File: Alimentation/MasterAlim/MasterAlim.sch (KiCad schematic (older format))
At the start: 37 parts, among them J1 Ext-Con, J10 Batt GND, J11 AU Logic, J2 Alim logique, J3 Batt IN, J4 Reg 1, J5 Batt +, J6 Reg 3, J7 Reg 4, J8 Reg 1, J9 Reg 2, U1 74LS33, U3 ACS712xLCTR-20A

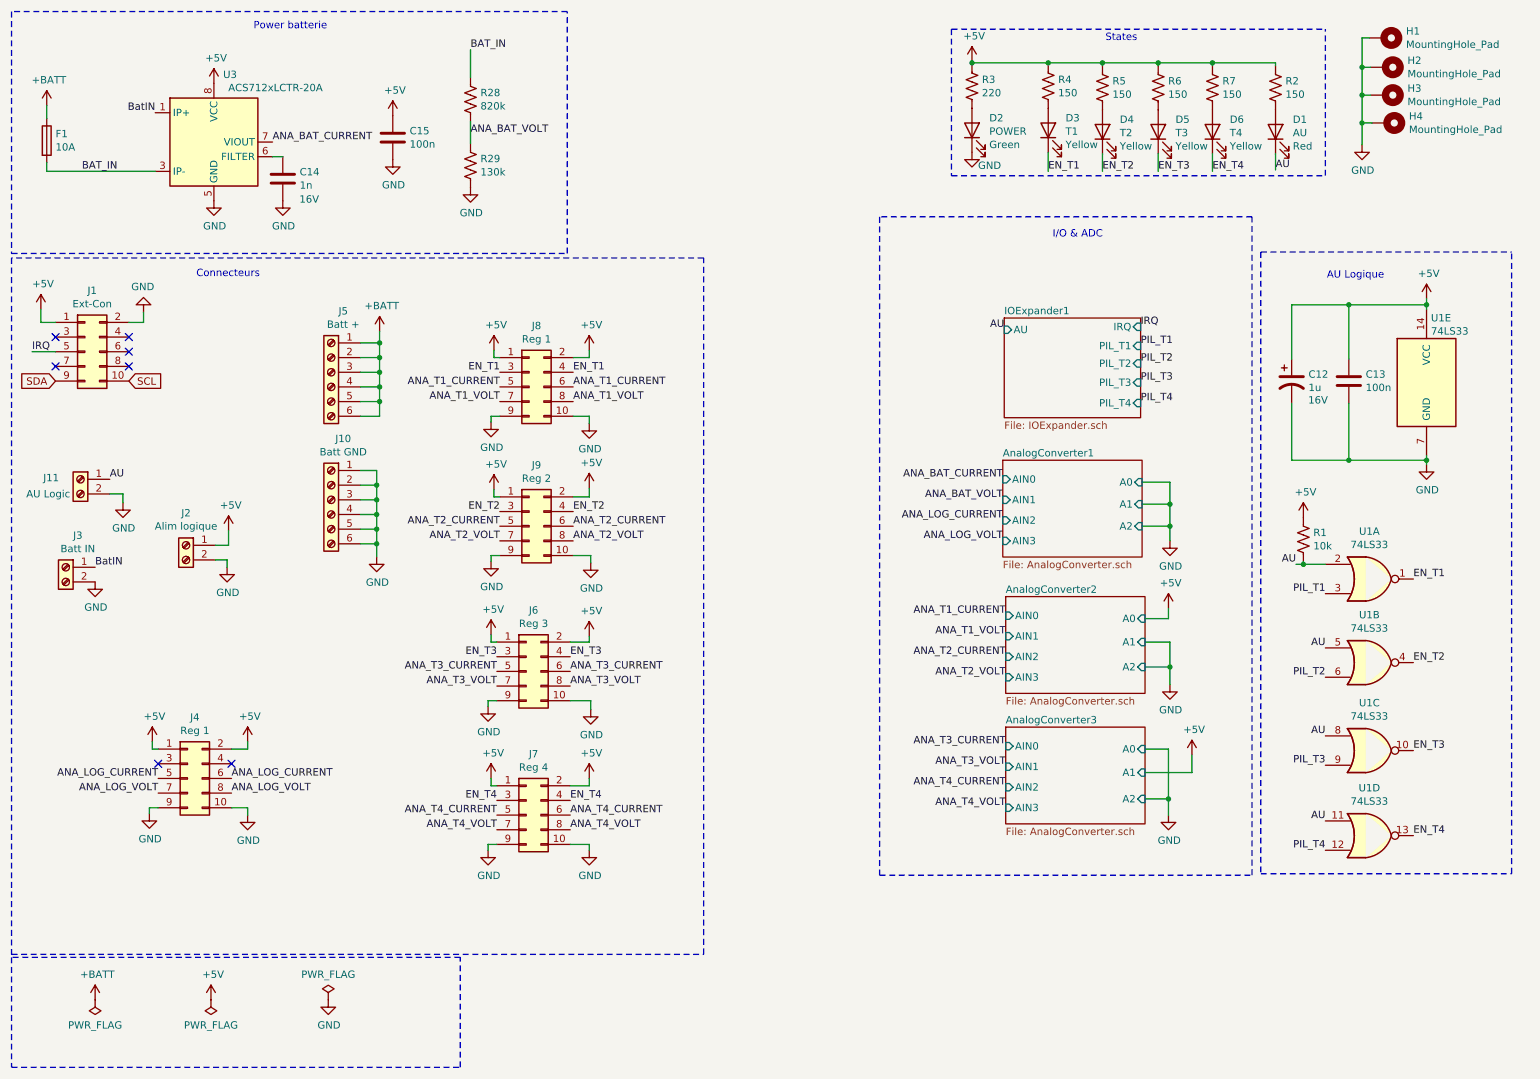
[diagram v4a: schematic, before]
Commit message: Finalisation modules 3A et 6A, routage master alim
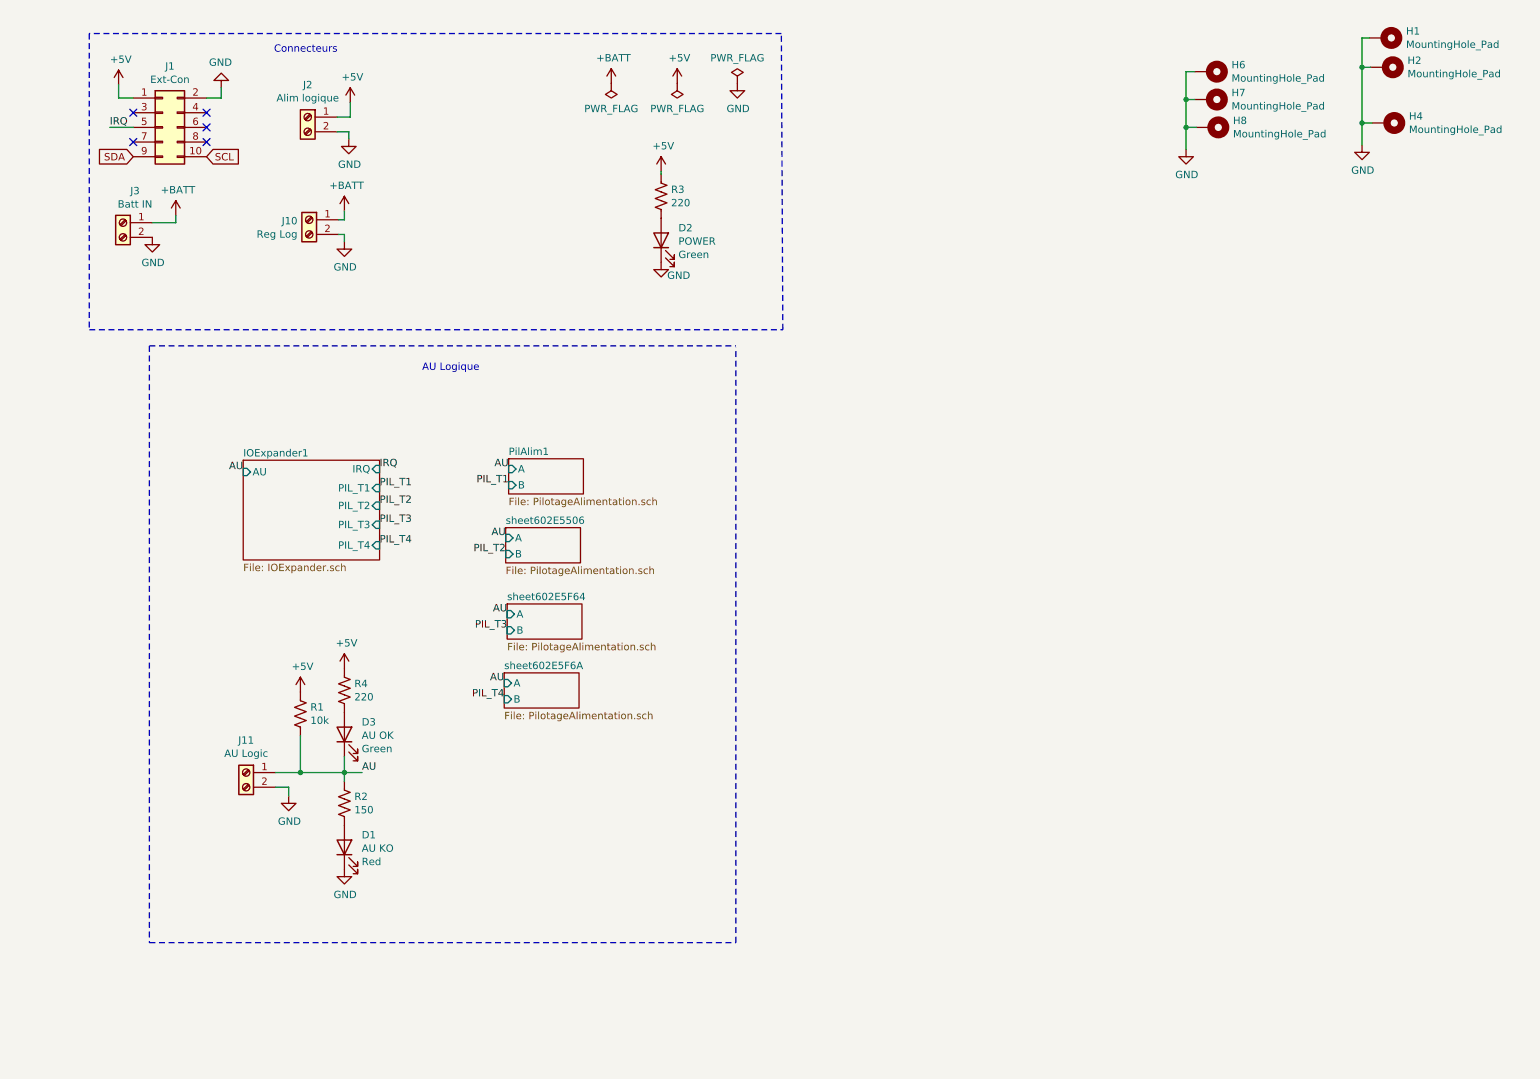
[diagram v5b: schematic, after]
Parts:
- removed C12: 1u, Capacitor_SMD:CP_Elec_4x5.3, symbol Device:CP1
- removed C13, C15: 100n, Capacitor_SMD:C_0603_1608Metric_Pad1.08x0.95mm_HandSolder, symbol Device:C
- removed C14: 1n, Capacitor_SMD:C_0603_1608Metric_Pad1.08x0.95mm_HandSolder, symbol Device:C
- removed D4: T2, LED_SMD:LED_0805_2012Metric, symbol Device:LED
- removed D5: T3, LED_SMD:LED_0805_2012Metric, symbol Device:LED
- removed D6: T4, LED_SMD:LED_0805_2012Metric, symbol Device:LED
- removed F1: 10A, Fuse:Fuseholder_Cylinder-5x20mm_Schurter_0031_8201_Horizontal_Open, symbol Device:Fuse
- removed H3: MountingHole_Pad, MountingHole:MountingHole_3.2mm_M3_Pad_Via, symbol Mechanical:MountingHole_Pad
- removed J10: Batt GND, TerminalBlock_Phoenix:TerminalBlock_Phoenix_MKDS-1,5-6-5.08_1x06_P5.08mm_Horizontal, symbol Connector:Screw_Terminal_01x06
- removed J4, J8: Reg 1, Connector_IDC:IDC-Header_2x05_P2.54mm_Vertical, symbol Connector_Generic:Conn_02x05_Odd_Even
- removed J5: Batt +, TerminalBlock_Phoenix:TerminalBlock_Phoenix_MKDS-1,5-6-5.08_1x06_P5.08mm_Horizontal, symbol Connector:Screw_Terminal_01x06
- removed J6: Reg 3, Connector_IDC:IDC-Header_2x05_P2.54mm_Vertical, symbol Connector_Generic:Conn_02x05_Odd_Even
- removed J7: Reg 4, Connector_IDC:IDC-Header_2x05_P2.54mm_Vertical, symbol Connector_Generic:Conn_02x05_Odd_Even
- removed J9: Reg 2, Connector_IDC:IDC-Header_2x05_P2.54mm_Vertical, symbol Connector_Generic:Conn_02x05_Odd_Even
- removed R28: 820k, Resistor_SMD:R_0805_2012Metric_Pad1.20x1.40mm_HandSolder, symbol Device:R_US
- removed R29: 130k, Resistor_SMD:R_0805_2012Metric_Pad1.20x1.40mm_HandSolder, symbol Device:R_US
- removed R5, R6, R7: 150, Resistor_SMD:R_0805_2012Metric_Pad1.20x1.40mm_HandSolder, symbol Device:R_US
- removed U1: 74LS33, Package_DIP:DIP-14_W7.62mm_Socket_LongPads, symbol 74xx:74LS33
- removed U3: ACS712xLCTR-20A, Package_SO:SOIC-8_3.9x4.9mm_P1.27mm, symbol Sensor_Current:ACS712xLCTR-20A
- added H6, H7, H8: MountingHole_Pad, MountingHole:MountingHole_3.2mm_M3_Pad_Via, symbol Mechanical:MountingHole_Pad
- added J10: Reg Log, TerminalBlock_Phoenix:TerminalBlock_Phoenix_MKDS-1,5-2-5.08_1x02_P5.08mm_Horizontal, symbol Connector:Screw_Terminal_01x02
- D1: value AU -> AU KO
- D3: value T1 -> AU OK; Color Yellow -> Green; LCSC Part C74346 -> C63855
- R4: value 150 -> 220; LCSC Part C17471 -> C417010
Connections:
- net BatIN is gone; now on net +BATT: J3.1 (Pin_1)
- net EN_T1 is gone; now on net AU: D3.1 (K)
- net +5V: no longer R2.1
- net +BATT: now also J10.1 (Pin_1)
- net AU: now also R2.1; no longer D1.1 (K)
- net GND: now also D1.1 (K), H6.1, H7.1, H8.1, J10.2 (Pin_2)
- no-connect marks 7 -> 5
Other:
- note removed: "I/O & ADC"
- note removed: "Power batterie\n"
- note removed: "States"
- moved on the sheet: D1, D2, J1, J11, J2, J3, R1, R2, R3

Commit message: Rework suite point robot
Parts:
- removed H6, H7, H8: MountingHole_Pad, MountingHole:MountingHole_3.2mm_M3_Pad_Via, symbol Mechanical:MountingHole_Pad
- added H3: MountingHole_Pad, MountingHole:MountingHole_3.2mm_M3_Pad_Via, symbol Mechanical:MountingHole_Pad
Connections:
- net GND: now also H3.1
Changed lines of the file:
@@
 	1    0    0    -1
 $EndComp
-$Comp
-L Mechanical:MountingHole_Pad H6
-U 1 1 5FFF4E9C
-P 9060 970
-F 0 "H6" V 9014 1120 50  0000 L CNN
-F 1 "MountingHole_Pad" V 9105 1120 50  0000 L CNN
-F 2 "MountingHole:MountingHole_3.2mm_M3_Pad_Via" H 9060 970 50  0001 C CNN
-F 3 "~" H 9060 970 50  0001 C CNN
-F 4 "0" H 9060 970 50  0001 C CNN "JLCPCB BOM"
-	1    9060 970
-	0    1    1    0
-$EndComp
-$Comp
-L Mechanical:MountingHole_Pad H7
-U 1 1 5FFF4EA7
-P 9060 1160
-F 0 "H7" V 9014 1310 50  0000 L CNN
-F 1 "MountingHole_Pad" V 9105 1310 50  0000 L CNN
-F 2 "MountingHole:MountingHole_3.2mm_M3_Pad_Via" H 9060 1160 50  0001 C CNN
-F 3 "~" H 9060 1160 50  0001 C CNN
-F 4 "0" H 9060 1160 50  0001 C CNN "JLCPCB BOM"
-	1    9060 1160
-	0    1    1    0
-$EndComp
-$Comp
-L Mechanical:MountingHole_Pad H8
-U 1 1 5FFF4EB2
-P 9070 1350
-F 0 "H8" V 9024 1500 50  0000 L CNN
-F 1 "MountingHole_Pad" V 9115 1500 50  0000 L CNN
-F 2 "MountingHole:MountingHole_3.2mm_M3_Pad_Via" H 9070 1350 50  0001 C CNN
-F 3 "~" H 9070 1350 50  0001 C CNN
-F 4 "0" H 9070 1350 50  0001 C CNN "JLCPCB BOM"
-	1    9070 1350
-	0    1    1    0
-$EndComp
-$Comp
-L power:GND #PWR06
-U 1 1 5FFF4EBC
-P 8900 1500
-F 0 "#PWR06" H 8900 1250 50  0001 C CNN
-F 1 "GND" H 8905 1327 50  0000 C CNN
-F 2 "" H 8900 1500 50  0001 C CNN
-F 3 "" H 8900 1500 50  0001 C CNN
-	1    8900 1500
-	1    0    0    -1
-$EndComp
-Wire Wire Line
-	8960 970  8900 970
-Wire Wire Line
-	8960 1160 8900 1160
-Connection ~ 8900 1160
-Wire Wire Line
-	8900 1160 8900 970
-Wire Wire Line
-	8970 1350 8900 1350
-Connection ~ 8900 1350
-Wire Wire Line
-	8900 1350 8900 1160
-Wire Wire Line
-	8900 1350 8900 1500
 Wire Wire Line
 	1850 2000 2010 2000
@@
 	2690 5750 2860 5750
 Wire Wire Line
-	10100 940  10100 1320
+	10100 940  10100 1130
+$Comp
+L Mechanical:MountingHole_Pad H3
+U 1 1 5FEFEFD7
+P 10260 1130
+F 0 "H3" V 10214 1280 50  0000 L CNN
+F 1 "MountingHole_Pad" V 10305 1280 50  0000 L CNN
+F 2 "MountingHole:MountingHole_3.2mm_M3_Pad_Via" H 10260 1130 50  0001 C CNN
+F 3 "~" H 10260 1130 50  0001 C CNN
+F 4 "0" H 10260 1130 50  0001 C CNN "JLCPCB BOM"
+	1    10260 1130
+	0    1    1    0
+$EndComp
+Wire Wire Line
+	10160 1130 10100 1130
+Connection ~ 10100 1130
+Wire Wire Line
+	10100 1130 10100 1320
 $EndSCHEMATC

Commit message: Finalisation alimentations
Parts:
- removed H4: MountingHole_Pad, MountingHole:MountingHole_3.2mm_M3_Pad_Via, symbol Mechanical:MountingHole_Pad
- removed J10: Reg Log, TerminalBlock_Phoenix:TerminalBlock_Phoenix_MKDS-1,5-2-5.08_1x02_P5.08mm_Horizontal, symbol Connector:Screw_Terminal_01x02
- removed J3: Batt IN, TerminalBlock_Phoenix:TerminalBlock_Phoenix_MKDS-1,5-2-5.08_1x02_P5.08mm_Horizontal, symbol Connector:Screw_Terminal_01x02
- added C1, C3: 1u, Capacitor_SMD:CP_Elec_4x5.3, symbol Device:CP1
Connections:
- net +5V: now also C1.1, C3.1
- net GND: now also C1.2, C3.2
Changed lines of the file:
@@
 $EndDescr
-$Comp
-L power:+BATT #PWR0101
-U 1 1 5FB579E7
-P 2010 1950
-F 0 "#PWR0101" H 2010 1800 50  0001 C CNN
-F 1 "+BATT" H 2025 2123 50  0000 C CNN
-F 2 "" H 2010 1950 50  0001 C CNN
-F 3 "" H 2010 1950 50  0001 C CNN
-	1    2010 1950
-	1    0    0    -1
-$EndComp
 $Comp
 L Connector_Generic:Conn_02x05_Odd_Even J1
@@
 Wire Notes Line
 	1830 2840 1830 6910
-$Comp
-L power:PWR_FLAG #FLG0101
-U 1 1 5FB5E21F
-P 4980 1050
-F 0 "#FLG0101" H 4980 1125 50  0001 C CNN
-F 1 "PWR_FLAG" H 4980 1223 50  0000 C CNN
-F 2 "" H 4980 1050 50  0001 C CNN
-F 3 "~" H 4980 1050 50  0001 C CNN
-	1    4980 1050
-	-1   0    0    1
-$EndComp
 $Comp
 L power:PWR_FLAG #FLG0103
@@
 Text Label 3400 4060 0    50   ~ 0
 PIL_T3
-$Comp
-L power:+BATT #PWR0112
-U 1 1 60077FA1
-P 4980 1050
-F 0 "#PWR0112" H 4980 900 50  0001 C CNN
-F 1 "+BATT" H 4995 1223 50  0000 C CNN
-F 2 "" H 4980 1050 50  0001 C CNN
-F 3 "" H 4980 1050 50  0001 C CNN
-	1    4980 1050
-	1    0    0    -1
-$EndComp
 $Comp
 L Connector:Screw_Terminal_01x02 J11
@@
 IRQ
 $Comp
-L power:GND #PWR03
-U 1 1 611B3F0A
-P 1850 2100
-F 0 "#PWR03" H 1850 1850 50  0001 C CNN
-F 1 "GND" H 1855 1927 50  0000 C CNN
-F 2 "" H 1850 2100 50  0001 C CNN
-F 3 "" H 1850 2100 50  0001 C CNN
-	1    1850 2100
-	1    0    0    -1
-$EndComp
-$Comp
 L power:PWR_FLAG #FLG0102
 U 1 1 5FD662F5
@@
 Wire Notes Line
 	1830 2840 5830 2840
-$Comp
-L Connector:Screw_Terminal_01x02 J3
-U 1 1 5FF5487A
-P 1650 2000
-F 0 "J3" H 1568 2217 50  0000 C CNN
-F 1 "Batt IN" H 1568 2126 50  0000 C CNN
-F 2 "TerminalBlock_Phoenix:TerminalBlock_Phoenix_MKDS-1,5-2-5.08_1x02_P5.08mm_Horizontal" H 1650 2000 50  0001 C CNN
-F 3 "~" H 1650 2000 50  0001 C CNN
-F 4 "0" H 1650 2000 50  0001 C CNN "JLCPCB BOM"
-	1    1650 2000
-	-1   0    0    -1
-$EndComp
 $Comp
 L Mechanical:MountingHole_Pad H1
@@
 $EndComp
 $Comp
-L Mechanical:MountingHole_Pad H4
-U 1 1 5FCE34CF
-P 10270 1320
-F 0 "H4" V 10224 1470 50  0000 L CNN
-F 1 "MountingHole_Pad" V 10315 1470 50  0000 L CNN
-F 2 "MountingHole:MountingHole_3.2mm_M3_Pad_Via" H 10270 1320 50  0001 C CNN
-F 3 "~" H 10270 1320 50  0001 C CNN
-F 4 "0" H 10270 1320 50  0001 C CNN "JLCPCB BOM"
-	1    10270 1320
-	0    1    1    0
-$EndComp
-$Comp
 L power:GND #PWR041
 U 1 1 5FCE38AF
-P 10100 1470
-F 0 "#PWR041" H 10100 1220 50  0001 C CNN
-F 1 "GND" H 10105 1297 50  0000 C CNN
-F 2 "" H 10100 1470 50  0001 C CNN
-F 3 "" H 10100 1470 50  0001 C CNN
-	1    10100 1470
+P 10100 1170
+F 0 "#PWR041" H 10100 920 50  0001 C CNN
+F 1 "GND" H 10105 997 50  0000 C CNN
+F 2 "" H 10100 1170 50  0001 C CNN
+F 3 "" H 10100 1170 50  0001 C CNN
+	1    10100 1170
 	1    0    0    -1
 $EndComp
@@
 Wire Wire Line
 	10100 940  10100 740
-Wire Wire Line
-	10170 1320 10100 1320
-Connection ~ 10100 1320
-Wire Wire Line
-	10100 1320 10100 1470
 Wire Wire Line
 	2690 5850 2780 5850
@@
 	-1   0    0    -1
 $EndComp
-Wire Wire Line
-	2010 2000 2010 1950
-$Comp
-L Connector:Screw_Terminal_01x02 J10
-U 1 1 5FFB6941
-P 2920 1980
-F 0 "J10" H 3000 1972 50  0000 L CNN
-F 1 "Reg Log" H 3000 1881 50  0000 L CNN
-F 2 "TerminalBlock_Phoenix:TerminalBlock_Phoenix_MKDS-1,5-2-5.08_1x02_P5.08mm_Horizontal" H 2920 1980 50  0001 C CNN
-F 3 "~" H 2920 1980 50  0001 C CNN
-F 4 "0" H 2920 1980 50  0001 C CNN "JLCPCB BOM"
-	1    2920 1980
-	-1   0    0    -1
-$EndComp
-$Comp
-L power:GND #PWR05
-U 1 1 5FFB830A
-P 3160 2130
-F 0 "#PWR05" H 3160 1880 50  0001 C CNN
-F 1 "GND" H 3165 1957 50  0000 C CNN
-F 2 "" H 3160 2130 50  0001 C CNN
-F 3 "" H 3160 2130 50  0001 C CNN
-	1    3160 2130
-	1    0    0    -1
-$EndComp
-$Comp
-L power:+BATT #PWR04
-U 1 1 5FFBA13B
-P 3160 1920
-F 0 "#PWR04" H 3160 1770 50  0001 C CNN
-F 1 "+BATT" H 3175 2093 50  0000 C CNN
-F 2 "" H 3160 1920 50  0001 C CNN
-F 3 "" H 3160 1920 50  0001 C CNN
-	1    3160 1920
-	1    0    0    -1
-$EndComp
-Wire Wire Line
-	1850 2000 2010 2000
 Text Label 3280 5750 0    50   ~ 0
 AU
 Wire Wire Line
 	5320 1650 5320 1670
-Wire Wire Line
-	3160 1920 3160 1980
-Wire Wire Line
-	3160 2130 3160 2080
-Wire Wire Line
-	3120 1980 3160 1980
-Wire Wire Line
-	3120 2080 3160 2080
 Text Label 4280 3680 2    50   ~ 0
 AU
@@
 	10160 1130 10100 1130
 Connection ~ 10100 1130
-Wire Wire Line
-	10100 1130 10100 1320
+$Comp
+L Device:CP1 C1
+U 1 1 5FE2AECF
+P 4390 6000
+AR Path="/5FE2AECF" Ref="C1"  Part="1"
+AR Path="/60C96C2B/5FE2AECF" Ref="C?"  Part="1"
+AR Path="/60167E1F/5FE2AECF" Ref="C?"  Part="1"
+AR Path="/602E5506/5FE2AECF" Ref="C?"  Part="1"
+AR Path="/602E5F64/5FE2AECF" Ref="C?"  Part="1"
+AR Path="/602E5F6A/5FE2AECF" Ref="C?"  Part="1"
+F 0 "C1" H 4505 6046 50  0000 L CNN
+F 1 "1u" H 4505 5955 50  0000 L CNN
+F 2 "Capacitor_SMD:CP_Elec_4x5.3" H 4390 6000 50  0001 C CNN
+F 3 "~" H 4390 6000 50  0001 C CNN
+F 4 "16V" H 4580 5870 50  0000 C CNN "Tension"
+F 5 "C249445" H 4390 6000 50  0001 C CNN "LCSC Part"
+	1    4390 6000
+	1    0    0    -1
+$EndComp
+$Comp
+L Device:CP1 C3
+U 1 1 5FE2B2E6
+P 4810 6010
+AR Path="/5FE2B2E6" Ref="C3"  Part="1"
+AR Path="/60C96C2B/5FE2B2E6" Ref="C?"  Part="1"
+AR Path="/60167E1F/5FE2B2E6" Ref="C?"  Part="1"
+AR Path="/602E5506/5FE2B2E6" Ref="C?"  Part="1"
+AR Path="/602E5F64/5FE2B2E6" Ref="C?"  Part="1"
+AR Path="/602E5F6A/5FE2B2E6" Ref="C?"  Part="1"
+F 0 "C3" H 4925 6056 50  0000 L CNN
+F 1 "1u" H 4925 5965 50  0000 L CNN
+F 2 "Capacitor_SMD:CP_Elec_4x5.3" H 4810 6010 50  0001 C CNN
+F 3 "~" H 4810 6010 50  0001 C CNN
+F 4 "16V" H 5000 5880 50  0000 C CNN "Tension"
+F 5 "C249445" H 4810 6010 50  0001 C CNN "LCSC Part"
+	1    4810 6010
+	1    0    0    -1
+$EndComp
+$Comp
+L power:GND #PWR04
+U 1 1 5FE2B8CD
+P 4390 6220
+F 0 "#PWR04" H 4390 5970 50  0001 C CNN
+F 1 "GND" H 4395 6047 50  0000 C CNN
+F 2 "" H 4390 6220 50  0001 C CNN
+F 3 "" H 4390 6220 50  0001 C CNN
+	1    4390 6220
+	1    0    0    -1
+$EndComp
+$Comp
+L power:+5V #PWR03
+U 1 1 5FE2BE52
+P 4390 5780
+F 0 "#PWR03" H 4390 5630 50  0001 C CNN
+F 1 "+5V" H 4405 5953 50  0000 C CNN
+F 2 "" H 4390 5780 50  0001 C CNN
+F 3 "" H 4390 5780 50  0001 C CNN
+	1    4390 5780
+	1    0    0    -1
+$EndComp
+Wire Wire Line
+	4810 6160 4810 6180
+Wire Wire Line
+	4810 6180 4390 6180
+Wire Wire Line
+	4390 6180 4390 6220
+Wire Wire Line
+	4390 6150 4390 6180
+Connection ~ 4390 6180
+Wire Wire Line
+	4390 5850 4390 5820
+Wire Wire Line
+	4390 5820 4810 5820
+Wire Wire Line
+	4810 5820 4810 5860
+Wire Wire Line
+	4390 5780 4390 5820
+Connection ~ 4390 5820
+Wire Wire Line
+	10100 1130 10100 1170
 $EndSCHEMATC

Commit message: Finalisation pour commande pack Alimentation 14/02/2021
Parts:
- C1, C3: footprint Capacitor_SMD:CP_Elec_4x5.3 -> Capacitor_THT:CP_Radial_D5.0mm_P2.50mm; JLCPCB BOM (none) -> 0; LCSC Part C249445 -> (none)
- R3, R4: LCSC Part C417010 -> C17557
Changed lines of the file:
@@
 F 2 "Resistor_SMD:R_0805_2012Metric_Pad1.20x1.40mm_HandSolder" V 5360 1810 50  0001 C CNN
 F 3 "~" H 5320 1820 50  0001 C CNN
-F 4 "C417010" H 5320 1820 50  0001 C CNN "LCSC Part"
+F 4 " C17557" H 5320 1820 50  0001 C CNN "LCSC Part"
 	1    5320 1820
 	1    0    0    -1
@@
 F 2 "Resistor_SMD:R_0805_2012Metric_Pad1.20x1.40mm_HandSolder" V 3200 5180 50  0001 C CNN
 F 3 "~" H 3160 5190 50  0001 C CNN
-F 4 "C417010" H 3160 5190 50  0001 C CNN "LCSC Part"
+F 4 " C17557" H 3160 5190 50  0001 C CNN "LCSC Part"
 	1    3160 5190
 	1    0    0    -1
@@
 F 0 "C1" H 4505 6046 50  0000 L CNN
 F 1 "1u" H 4505 5955 50  0000 L CNN
-F 2 "Capacitor_SMD:CP_Elec_4x5.3" H 4390 6000 50  0001 C CNN
+F 2 "Capacitor_THT:CP_Radial_D5.0mm_P2.50mm" H 4390 6000 50  0001 C CNN
 F 3 "~" H 4390 6000 50  0001 C CNN
 F 4 "16V" H 4580 5870 50  0000 C CNN "Tension"
-F 5 "C249445" H 4390 6000 50  0001 C CNN "LCSC Part"
+F 5 "" H 4390 6000 50  0001 C CNN "LCSC Part"
+F 6 "0" H 4390 6000 50  0001 C CNN "JLCPCB BOM"
 	1    4390 6000
 	1    0    0    -1
@@
 F 0 "C3" H 4925 6056 50  0000 L CNN
 F 1 "1u" H 4925 5965 50  0000 L CNN
-F 2 "Capacitor_SMD:CP_Elec_4x5.3" H 4810 6010 50  0001 C CNN
+F 2 "Capacitor_THT:CP_Radial_D5.0mm_P2.50mm" H 4810 6010 50  0001 C CNN
 F 3 "~" H 4810 6010 50  0001 C CNN
 F 4 "16V" H 5000 5880 50  0000 C CNN "Tension"
-F 5 "C249445" H 4810 6010 50  0001 C CNN "LCSC Part"
+F 5 "" H 4810 6010 50  0001 C CNN "LCSC Part"
+F 6 "0" H 4810 6010 50  0001 C CNN "JLCPCB BOM"
 	1    4810 6010
 	1    0    0    -1
